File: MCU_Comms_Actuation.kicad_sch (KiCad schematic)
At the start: 42 parts, among them J1 MTSW-105-09-L-S-480, Y1 Crystal

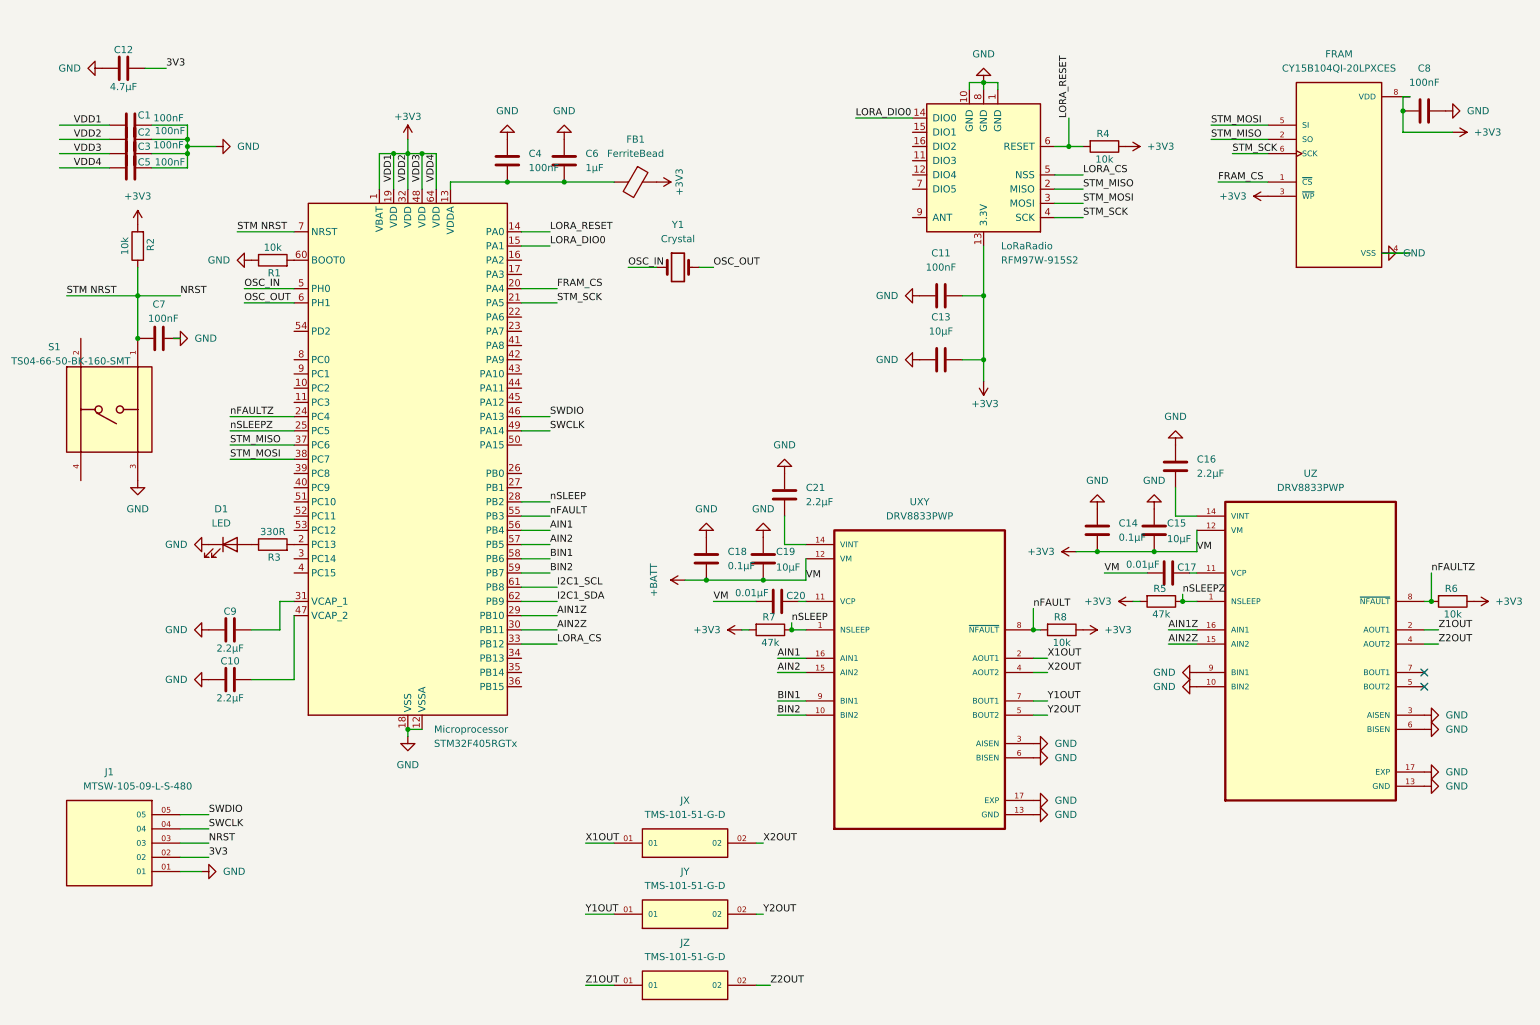
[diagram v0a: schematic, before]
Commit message: Correct SPI labelling
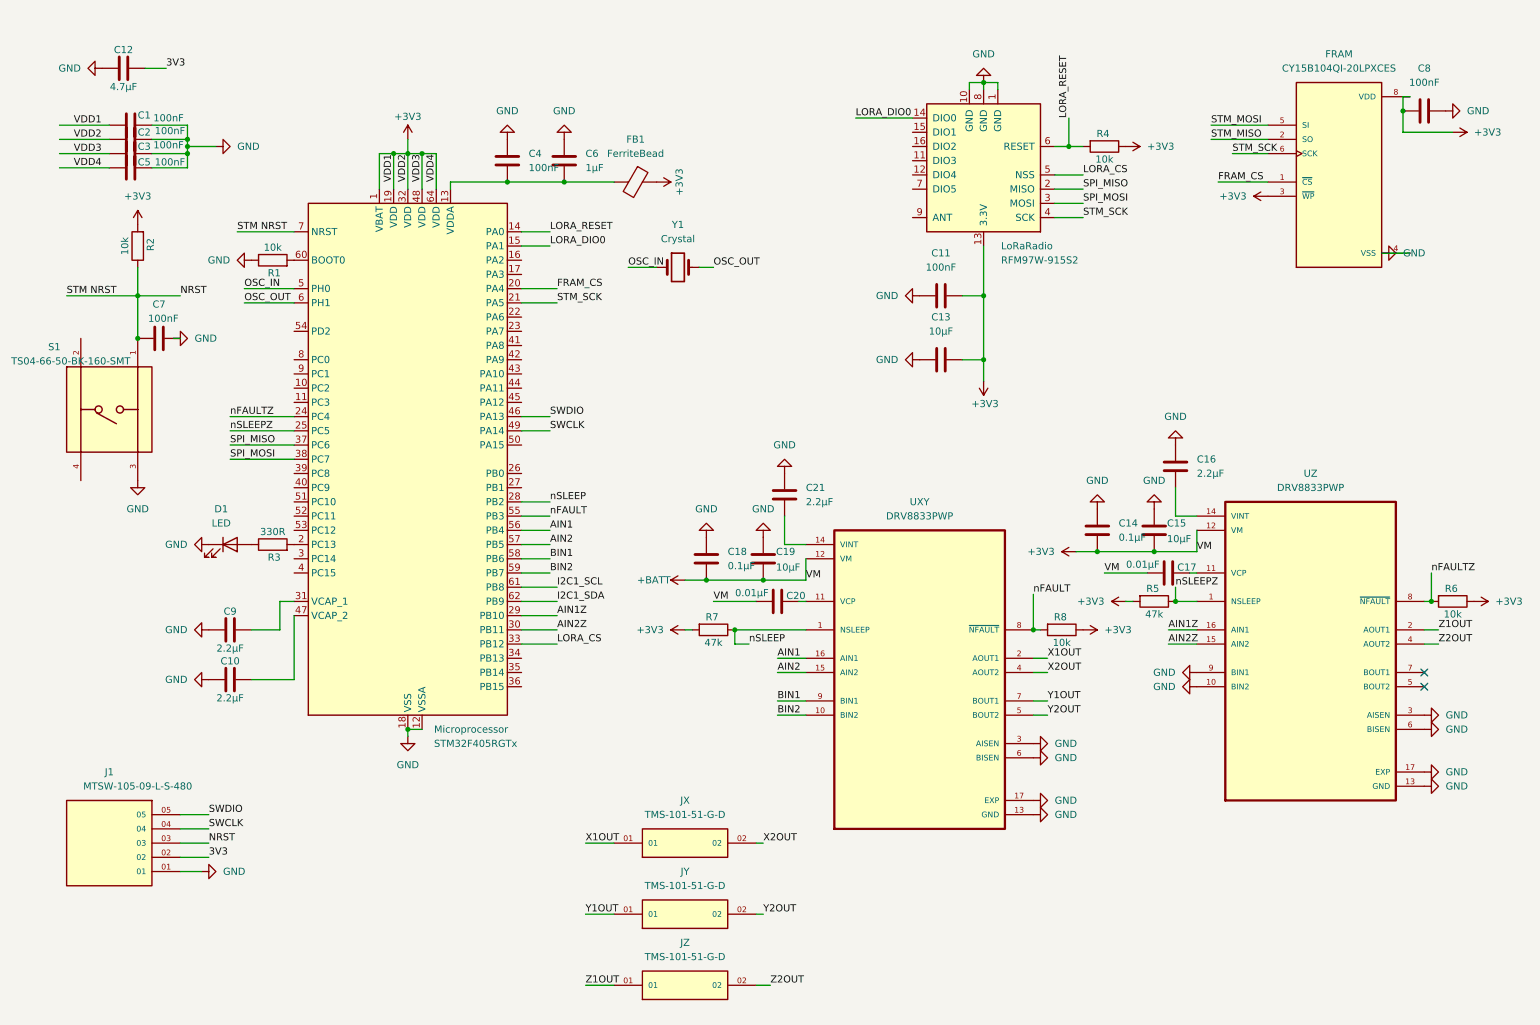
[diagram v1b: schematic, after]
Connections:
- net STM_MISO: no longer LoRaRadio.2 (MISO), Microprocessor.37 (PC6)
- net STM_MOSI: no longer LoRaRadio.3 (MOSI), Microprocessor.38 (PC7)
- new net SPI_MISO: LoRaRadio.2 (MISO), Microprocessor.37 (PC6)
- new net SPI_MOSI: LoRaRadio.3 (MOSI), Microprocessor.38 (PC7)
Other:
- moved on the sheet: R5, R7
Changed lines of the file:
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@@
 	)
 	(junction
-		(at 222.25 119.38)
-		(diameter 0)
-		(color 0 0 0 0)
-	)
-	(junction
 		(at 81.28 39.37)
 		(diameter 0)
@@
 	)
 	(junction
-		(at 195.58 124.46)
-		(diameter 0)
-		(color 0 0 0 0)
-	)
-	(junction
 		(at 186.69 26.67)
 		(diameter 0)
@@
 	)
 	(junction
+		(at 220.98 119.38)
+		(diameter 0)
+		(color 0 0 0 0)
+	)
+	(junction
 		(at 137.16 115.57)
 		(diameter 0)
@@
 	)
 	(junction
-		(at 83.82 39.37)
+		(at 195.58 124.46)
 		(diameter 0)
 		(color 0 0 0 0)
 	)
 	(junction
-		(at 207.01 110.49)
+		(at 83.82 39.37)
 		(diameter 0)
 		(color 0 0 0 0)
 	)
 	(junction
-		(at 152.4 124.46)
+		(at 207.01 110.49)
 		(diameter 0)
 		(color 0 0 0 0)
@@
 	)
 	(junction
+		(at 142.24 124.46)
+		(diameter 0)
+		(color 0 0 0 0)
+	)
+	(junction
 		(at 186.69 76.2)
 		(diameter 0)
@@
 	(wire
 		(pts
-			(xy 195.58 120.65) (xy 195.58 124.46)
+			(xy 195.58 118.11) (xy 195.58 124.46)
 		)
 		(stroke
@@
 	(wire
 		(pts
-			(xy 152.4 124.46) (xy 154.94 124.46)
+			(xy 142.24 124.46) (xy 154.94 124.46)
 		)
 		(stroke
@@
 	(wire
 		(pts
-			(xy 152.4 123.19) (xy 152.4 124.46)
-		)
-		(stroke
-			(width 0)
-			(type default)
-		)
-	)
-	(wire
-		(pts
 			(xy 265.43 124.46) (xy 267.97 124.46)
 		)
@@
 	(wire
 		(pts
-			(xy 222.25 119.38) (xy 224.79 119.38)
+			(xy 220.98 119.38) (xy 224.79 119.38)
 		)
 		(stroke
@@
 	(wire
 		(pts
-			(xy 222.25 118.11) (xy 222.25 119.38)
+			(xy 220.98 116.84) (xy 220.98 119.38)
 		)
 		(stroke
@@
 	(wire
 		(pts
-			(xy 213.36 119.38) (xy 214.63 119.38)
+			(xy 212.09 119.38) (xy 213.36 119.38)
+		)
+		(stroke
+			(width 0)
+			(type default)
+		)
+	)
+	(wire
+		(pts
+			(xy 144.78 127) (xy 142.24 127)
 		)
 		(stroke
@@
 	(wire
 		(pts
+			(xy 142.24 127) (xy 142.24 124.46)
+		)
+		(stroke
+			(width 0)
+			(type default)
+		)
+	)
+	(wire
+		(pts
 			(xy 35.56 59.69) (xy 35.56 64.77)
 		)
@@
 	(wire
 		(pts
-			(xy 143.51 124.46) (xy 144.78 124.46)
+			(xy 133.35 124.46) (xy 134.62 124.46)
 		)
 		(stroke
@@
 	)
 	(label "nSLEEP"
-		(at 152.4 123.19 0)
+		(at 144.78 127 0)
 		(effects
 			(font
@@
 		)
 	)
-	(label "STM_MISO"
+	(label "SPI_MISO"
 		(at 52.07 91.44 0)
 		(effects
@@
 	)
 	(label "nFAULT"
-		(at 195.58 120.65 0)
+		(at 195.58 118.11 0)
 		(effects
 			(font
@@
 		)
 	)
-	(label "STM_MOSI"
+	(label "SPI_MOSI"
 		(at 52.07 93.98 0)
 		(effects
@@
 		)
 	)
-	(label "STM_MOSI"
+	(label "SPI_MOSI"
 		(at 204.47 48.26 0)
 		(effects
@@
 		)
 	)
-	(label "STM_MISO"
+	(label "SPI_MISO"
 		(at 204.47 45.72 0)
 		(effects
@@
 	)
 	(label "nSLEEPZ"
-		(at 222.25 118.11 0)
+		(at 220.98 116.84 0)
 		(effects
 			(font
@@
 	(symbol
 		(lib_id "Device:R")
-		(at 218.44 119.38 270)
+		(at 217.17 119.38 270)
 		(unit 1)
 		(body_style 1)
@@
 		(dnp no)
 		(property "Reference" "R5"
-			(at 218.186 117.094 90)
+			(at 216.916 117.094 90)
 			(show_name no)
 			(do_not_autoplace no)
@@
 		)
 		(property "Value" "47k"
-			(at 218.44 121.666 90)
+			(at 217.17 121.666 90)
 			(show_name no)
 			(do_not_autoplace no)
@@
 		)
 		(property "Footprint" ""
-			(at 218.44 117.602 90)
+			(at 217.17 117.602 90)
 			(hide yes)
 			(show_name no)
@@
 		)
 		(property "Datasheet" ""
-			(at 218.44 119.38 0)
+			(at 217.17 119.38 0)
 			(hide yes)
 			(show_name no)
@@
 		)
 		(property "Description" "Resistor"
-			(at 218.44 119.38 0)
+			(at 217.17 119.38 0)
 			(hide yes)
 			(show_name no)
@@
 	(symbol
 		(lib_id "power:+3V3")
-		(at 213.36 119.38 90)
+		(at 212.09 119.38 90)
 		(unit 1)
 		(body_style 1)
@@
 		(fields_autoplaced yes)
 		(property "Reference" "#PWR026"
-			(at 217.17 119.38 0)
+			(at 215.9 119.38 0)
 			(hide yes)
 			(show_name no)
@@
 		)
 		(property "Value" "+3V3"
-			(at 209.55 119.3799 90)
+			(at 208.28 119.3799 90)
 			(show_name no)
 			(do_not_autoplace no)
@@
 		)
 		(property "Footprint" ""
-			(at 213.36 119.38 0)
+			(at 212.09 119.38 0)
 			(hide yes)
 			(show_name no)
@@
 		)
 		(property "Datasheet" ""
-			(at 213.36 119.38 0)
+			(at 212.09 119.38 0)
 			(hide yes)
 			(show_name no)
@@
 		)
 		(property "Description" "Power symbol creates a global label with name \"+3V3\""
-			(at 213.36 119.38 0)
+			(at 212.09 119.38 0)
 			(hide yes)
 			(show_name no)
@@
 	(symbol
 		(lib_id "power:+3V3")
-		(at 143.51 124.46 90)
+		(at 133.35 124.46 90)
 		(unit 1)
 		(body_style 1)
@@
 		(fields_autoplaced yes)
 		(property "Reference" "#PWR035"
-			(at 147.32 124.46 0)
+			(at 137.16 124.46 0)
 			(hide yes)
 			(show_name no)
@@
 		)
 		(property "Value" "+3V3"
-			(at 139.7 124.4599 90)
+			(at 129.54 124.4599 90)
 			(show_name no)
 			(do_not_autoplace no)
@@
 		)
 		(property "Footprint" ""
-			(at 143.51 124.46 0)
+			(at 133.35 124.46 0)
 			(hide yes)
 			(show_name no)
@@
 		)
 		(property "Datasheet" ""
-			(at 143.51 124.46 0)
+			(at 133.35 124.46 0)
 			(hide yes)
 			(show_name no)
@@
 		)
 		(property "Description" "Power symbol creates a global label with name \"+3V3\""
-			(at 143.51 124.46 0)
+			(at 133.35 124.46 0)
 			(hide yes)
 			(show_name no)
@@
 	(symbol
 		(lib_id "Device:R")
-		(at 148.59 124.46 270)
+		(at 138.43 124.46 270)
 		(unit 1)
 		(body_style 1)
@@
 		(dnp no)
 		(property "Reference" "R7"
-			(at 148.336 122.174 90)
+			(at 138.176 122.174 90)
 			(show_name no)
 			(do_not_autoplace no)
@@
 		)
 		(property "Value" "47k"
-			(at 148.59 126.746 90)
+			(at 138.43 126.746 90)
 			(show_name no)
 			(do_not_autoplace no)
@@
 		)
 		(property "Footprint" ""
-			(at 148.59 122.682 90)
+			(at 138.43 122.682 90)
 			(hide yes)
 			(show_name no)
@@
 		)
 		(property "Datasheet" ""
-			(at 148.59 124.46 0)
+			(at 138.43 124.46 0)
 			(hide yes)
 			(show_name no)
@@
 		)
 		(property "Description" "Resistor"
-			(at 148.59 124.46 0)
+			(at 138.43 124.46 0)
 			(hide yes)
 			(show_name no)
@@
 		)
 		(property "Value" "+BATT"
-			(at 127.762 115.57 0)
+			(at 127.762 115.57 90)
 			(show_name no)
 			(do_not_autoplace no)

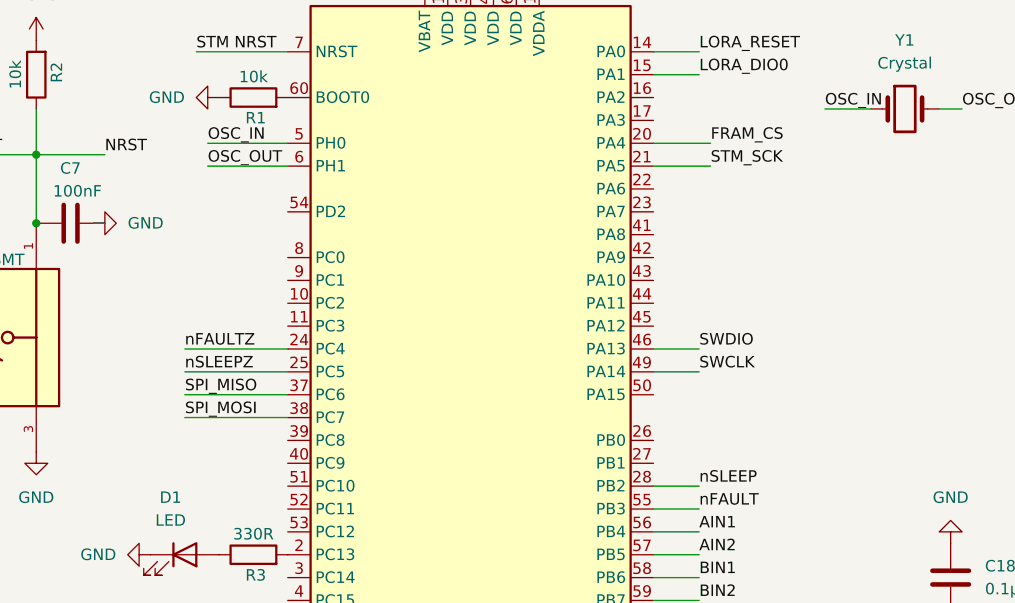
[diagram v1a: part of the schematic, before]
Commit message: Added Hierarchical Labels in MCU sheet for SPI_MISO, SPI_MOSI, SPI_CLK
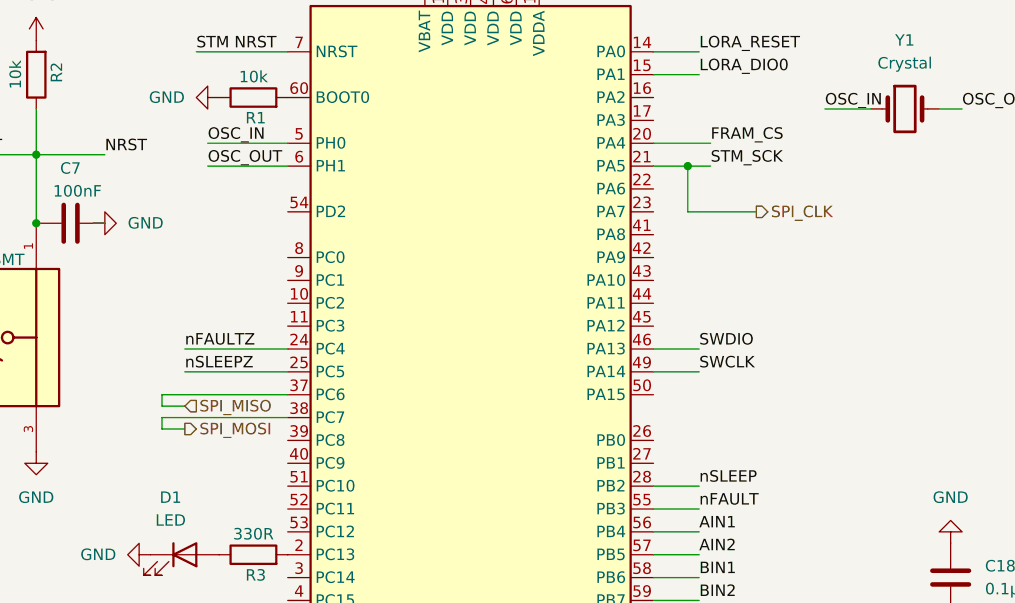
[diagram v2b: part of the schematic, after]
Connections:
- net STM_SCK renamed SPI_CLK
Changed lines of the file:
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@@
+	)
+	(junction
+		(at 107.95 66.04)
+		(diameter 0)
+		(color 0 0 0 0)
 	)
 	(junction
@@
 	(wire
 		(pts
+			(xy 49.53 95.25) (xy 49.53 93.98)
+		)
+		(stroke
+			(width 0)
+			(type default)
+		)
+	)
+	(wire
+		(pts
 			(xy 182.88 64.77) (xy 186.69 64.77)
 		)
@@
 	(wire
 		(pts
-			(xy 104.14 66.04) (xy 110.49 66.04)
+			(xy 104.14 66.04) (xy 107.95 66.04)
+		)
+		(stroke
+			(width 0)
+			(type default)
+		)
+	)
+	(wire
+		(pts
+			(xy 49.53 91.44) (xy 49.53 92.71)
 		)
 		(stroke
@@
 	(wire
 		(pts
+			(xy 107.95 71.12) (xy 115.57 71.12)
+		)
+		(stroke
+			(width 0)
+			(type default)
+		)
+	)
+	(wire
+		(pts
 			(xy 104.14 114.3) (xy 109.22 114.3)
 		)
@@
 	(wire
 		(pts
+			(xy 49.53 91.44) (xy 63.5 91.44)
+		)
+		(stroke
+			(width 0)
+			(type default)
+		)
+	)
+	(wire
+		(pts
 			(xy 186.69 64.77) (xy 186.69 76.2)
 		)
@@
 	(wire
 		(pts
-			(xy 52.07 91.44) (xy 63.5 91.44)
-		)
-		(stroke
-			(width 0)
-			(type default)
-		)
-	)
-	(wire
-		(pts
 			(xy 265.43 127) (xy 267.97 127)
 		)
@@
 	(wire
 		(pts
+			(xy 107.95 66.04) (xy 107.95 71.12)
+		)
+		(stroke
+			(width 0)
+			(type default)
+		)
+	)
+	(wire
+		(pts
 			(xy 43.18 165.1) (xy 48.26 165.1)
 		)
@@
 	(wire
 		(pts
+			(xy 49.53 92.71) (xy 52.07 92.71)
+		)
+		(stroke
+			(width 0)
+			(type default)
+		)
+	)
+	(wire
+		(pts
 			(xy 220.98 99.06) (xy 220.98 104.14)
 		)
@@
 	(wire
 		(pts
+			(xy 49.53 93.98) (xy 63.5 93.98)
+		)
+		(stroke
+			(width 0)
+			(type default)
+		)
+	)
+	(wire
+		(pts
 			(xy 44.45 39.37) (xy 44.45 41.91)
 		)
@@
 	(wire
 		(pts
-			(xy 52.07 93.98) (xy 63.5 93.98)
+			(xy 107.95 66.04) (xy 110.49 66.04)
 		)
 		(stroke
@@
 		(pts
 			(xy 142.24 127) (xy 142.24 124.46)
+		)
+		(stroke
+			(width 0)
+			(type default)
+		)
+	)
+	(wire
+		(pts
+			(xy 52.07 95.25) (xy 49.53 95.25)
 		)
 		(stroke
@@
 		)
 	)
-	(label "SPI_MISO"
-		(at 52.07 91.44 0)
-		(effects
-			(font
-				(size 1.27 1.27)
-			)
-			(justify left bottom)
-		)
-	)
 	(label "nFAULT"
 		(at 109.22 104.14 0)
@@
 		)
 	)
-	(label "SPI_MOSI"
-		(at 52.07 93.98 0)
-		(effects
-			(font
-				(size 1.27 1.27)
-			)
-			(justify left bottom)
-		)
-	)
 	(label "3V3"
 		(at 48.26 165.1 0)
@@
 		)
 	)
+	(hierarchical_label "SPI_CLK"
+		(shape output)
+		(at 115.57 71.12 0)
+		(effects
+			(font
+				(size 1.27 1.27)
+			)
+			(justify left)
+		)
+	)
+	(hierarchical_label "SPI_MISO"
+		(shape input)
+		(at 52.07 92.71 0)
+		(effects
+			(font
+				(size 1.27 1.27)
+			)
+			(justify left)
+		)
+	)
+	(hierarchical_label "SPI_MOSI"
+		(shape output)
+		(at 52.07 95.25 0)
+		(effects
+			(font
+				(size 1.27 1.27)
+			)
+			(justify left)
+		)
+	)
